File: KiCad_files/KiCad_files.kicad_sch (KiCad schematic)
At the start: 0 parts

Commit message: blablabla
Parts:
- added C1: 100nF, symbol Device:C
- added U1: ~, symbol New_Library:REF2033AIDDCT
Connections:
- new net: C1.1, U1. (V_REF)
- new net GND: C1.2, U1. (V_REF)

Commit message: test
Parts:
- added C2: 100nF, symbol Device:C
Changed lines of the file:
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@@
+	(symbol
+		(lib_id "Device:C")
+		(at 176.53 97.79 0)
+		(unit 1)
+		(exclude_from_sim no)
+		(in_bom yes)
+		(on_board yes)
+		(dnp no)
+		(fields_autoplaced yes)
+		(property "Reference" "C2"
+			(at 180.34 96.5199 0)
+			(effects
+				(font
+					(size 1.27 1.27)
+				)
+				(justify left)
+			)
+		)
+		(property "Value" "100nF"
+			(at 180.34 99.0599 0)
+			(effects
+				(font
+					(size 1.27 1.27)
+				)
+				(justify left)
+			)
+		)
+		(property "Footprint" ""
+			(at 177.4952 101.6 0)
+			(effects
+				(font
+					(size 1.27 1.27)
+				)
+				(hide yes)
+			)
+		)
+		(property "Datasheet" "~"
+			(at 176.53 97.79 0)
+			(effects
+				(font
+					(size 1.27 1.27)
+				)
+				(hide yes)
+			)
+		)
+		(property "Description" "Unpolarized capacitor"
+			(at 176.53 97.79 0)
+			(effects
+				(font
+					(size 1.27 1.27)
+				)
+				(hide yes)
+			)
+		)
+		(pin "2"
+		)
+		(pin "1"
+		)
+		(instances
+			(project "KiCad_files"
+				(path "/f93895fa-12b9-4ad7-81f4-36be00b56edd"
+					(reference "C2")
+					(unit 1)
+				)
+			)
+		)
+	)
 	(symbol
 		(lib_id "Device:C")

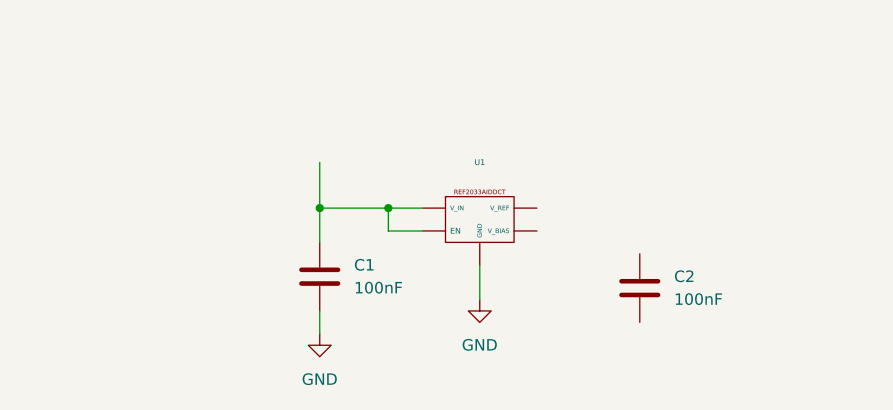
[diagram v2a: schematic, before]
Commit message: added the analog power supply to the main scheme
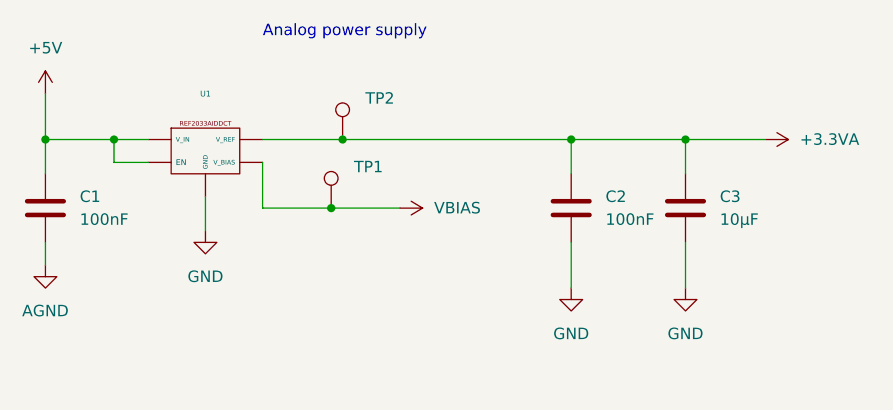
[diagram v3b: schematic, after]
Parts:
- added C3: 10μF, symbol Device:C
- added TP1, TP2: ~, symbol Connector:TestPoint
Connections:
- net GND: now also C2.2, C3.2; no longer C1.2
- net +3.3VA: now reaches C2.1
- net +3.3VA: now also U1. (V_REF), C3.1, TP2.1
- net +5V: now reaches C1.1, U1. (V_REF)
- net VBIAS: now reaches U1. (V_REF)
- net VBIAS: now also TP1.1
- new net AGND: C1.2
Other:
- note added: "Analog power supply"

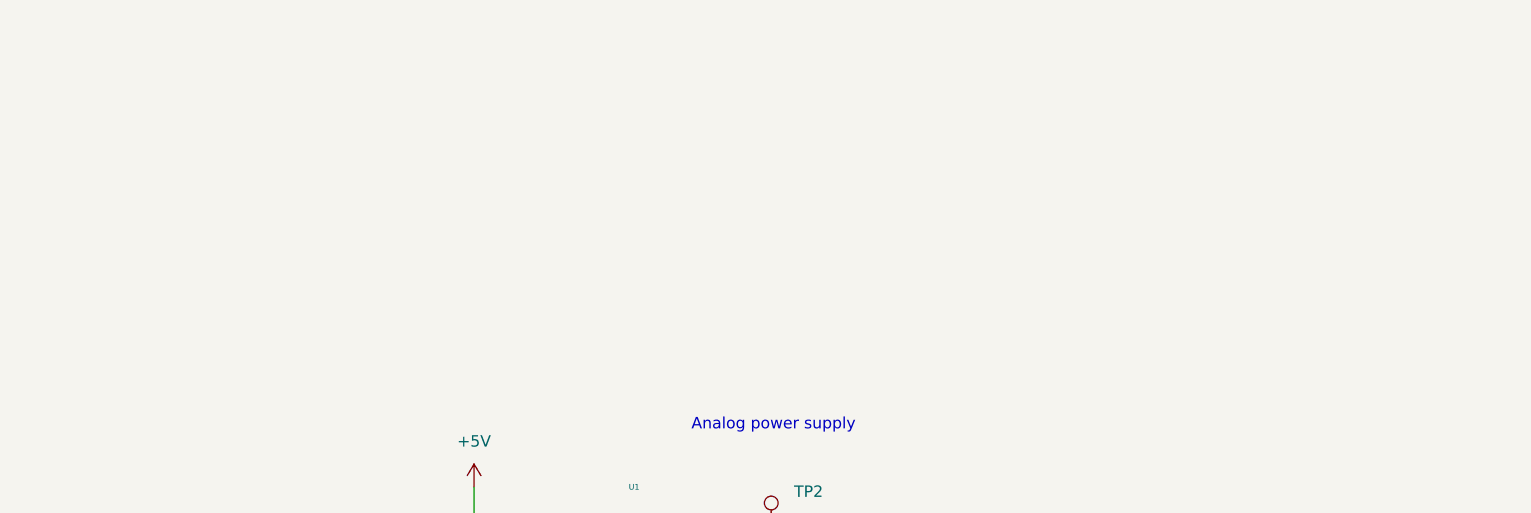
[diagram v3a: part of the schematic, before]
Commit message: Added digital power supply to schematic
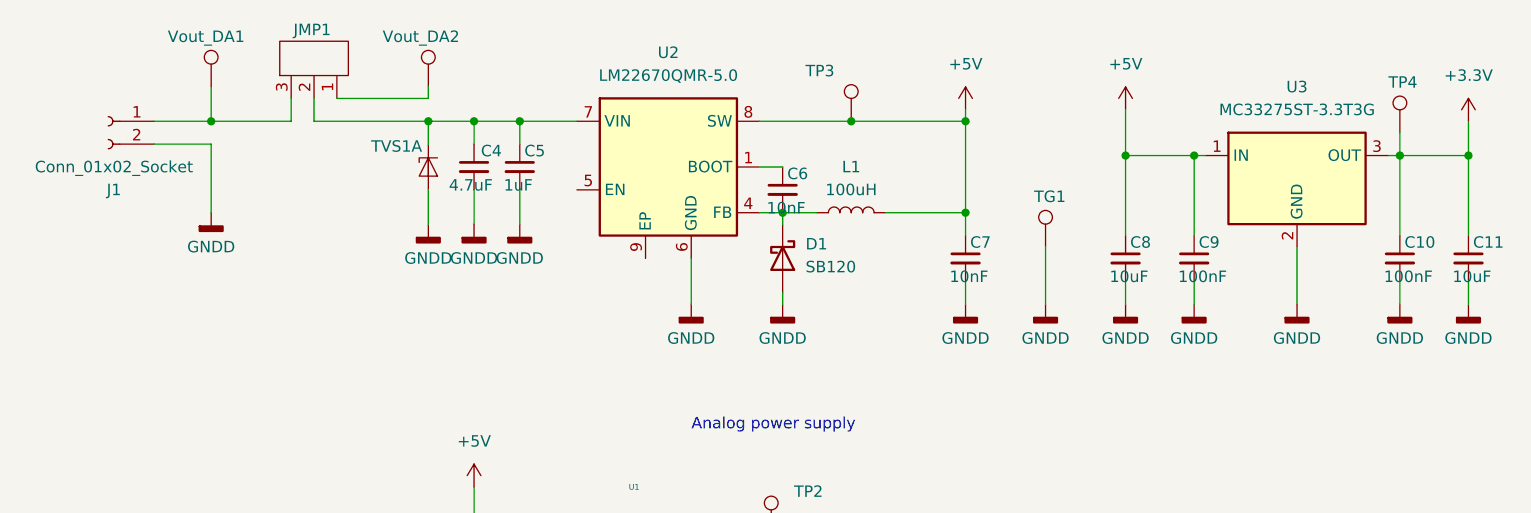
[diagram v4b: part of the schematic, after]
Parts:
- added C10, C9: 100nF, symbol Device:C_Small
- added C11, C8: 10uF, symbol Device:C_Small
- added C4: 4.7uF, symbol Device:C_Small
- added C5: 1uF, symbol Device:C_Small
- added C6, C7: 10nF, symbol Device:C_Small
- added D1: SB120, Diode_THT:D_DO-41_SOD81_P10.16mm_Horizontal, symbol Diode:SB120
- added J1: Conn_01x02_Socket, symbol Connector:Conn_01x02_Socket
- added JMP1: ~, symbol New_Library:3pin_jumper
- added L1: 100uH, symbol Device:L
- added TG1, TP3, TP4, Vout_DA1, Vout_DA2: TestPoint, symbol Connector:TestPoint
- added TVS1: PESD3V3U1UT, Package_TO_SOT_SMD:SOT-23, symbol Power_Protection:PESD3V3L4UF
- added U2: LM22670QMR-5.0, Package_SO:SOIC-8-1EP_3.9x4.9mm_P1.27mm_EP2.29x3mm, symbol Regulator_Switching:LM22676MR-5
- added U3: MC33275ST-3.3T3G, Package_TO_SOT_SMD:SOT-223, symbol Regulator_Linear:LT1963AxST-3.3
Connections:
- net +5V: now also C7.1, C8.1, C9.1, L1.2, TP3.1, U2.8 (SW), U3.1 (IN)
- new net: C4.1, C5.1, JMP1.2, TVS1.1 (K1), U2.7 (VIN)
- new net: JMP1.1, Vout_DA2.1
- new net: J1.1 (Pin_1), JMP1.3, Vout_DA1.1
- new net: C6.1, U2.1 (BOOT)
- new net: C6.2, D1.1 (K), L1.1, U2.4 (FB)
- new net +3.3V: C10.1, C11.1, TP4.1, U3.3 (OUT)
- new net GNDD: C10.2, C11.2, C4.2, C5.2, C7.2, C8.2, C9.2, D1.2 (A), J1.2 (Pin_2), TG1.1, TVS1.2 (A), TVS1.5 (A), U2.6 (GND), U3.2 (GND)

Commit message: minimal changes
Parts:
- removed Vout_DA1, Vout_DA2: TestPoint, symbol Connector:TestPoint
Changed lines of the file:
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@@
 	(wire
 		(pts
-			(xy 95.25 33.02) (xy 105.41 33.02)
+			(xy 95.25 33.02) (xy 101.6 33.02)
 		)
 		(stroke
@@
 	(wire
 		(pts
-			(xy 105.41 33.02) (xy 105.41 31.75)
+			(xy 101.6 33.02) (xy 101.6 30.48)
 		)
 		(stroke
@@
 	(wire
 		(pts
-			(xy 81.28 35.56) (xy 81.28 31.75)
+			(xy 81.28 35.56) (xy 81.28 30.48)
 		)
 		(stroke
@@
 		)
 	)
+	(netclass_flag ""
+		(length 2.54)
+		(shape round)
+		(at 101.6 30.48 0)
+		(effects
+			(font
+				(size 1.27 1.27)
+			)
+			(justify left bottom)
+		)
+		(property "Vin_DA15" ""
+			(at 96.774 25.908 0)
+			(show_name yes)
+			(effects
+				(font
+					(size 1.27 1.27)
+					(italic yes)
+				)
+				(justify left)
+			)
+		)
+	)
+	(netclass_flag ""
+		(length 2.54)
+		(shape round)
+		(at 81.28 30.48 0)
+		(effects
+			(font
+				(size 1.27 1.27)
+			)
+			(justify left bottom)
+		)
+		(property "Vout_DA15" ""
+			(at 75.946 25.908 0)
+			(show_name yes)
+			(effects
+				(font
+					(size 1.27 1.27)
+					(italic yes)
+				)
+				(justify left)
+			)
+		)
+	)
 	(symbol
 		(lib_id "power:GND")
@@
 	)
 	(symbol
-		(lib_id "Connector:TestPoint")
-		(at 105.41 31.75 0)
-		(unit 1)
-		(exclude_from_sim no)
-		(in_bom yes)
-		(on_board yes)
-		(dnp no)
-		(property "Reference" "Vout_DA2"
-			(at 100.33 26.162 0)
-			(effects
-				(font
-					(size 1.27 1.27)
-				)
-				(justify left)
-			)
-		)
-		(property "Value" "TestPoint"
-			(at 107.95 29.7179 0)
-			(effects
-				(font
-					(size 1.27 1.27)
-				)
-				(justify left)
-				(hide yes)
-			)
-		)
-		(property "Footprint" ""
-			(at 110.49 31.75 0)
-			(effects
-				(font
-					(size 1.27 1.27)
-				)
-				(hide yes)
-			)
-		)
-		(property "Datasheet" "~"
-			(at 110.49 31.75 0)
-			(effects
-				(font
-					(size 1.27 1.27)
-				)
-				(hide yes)
-			)
-		)
-		(property "Description" "test point"
-			(at 105.41 31.75 0)
-			(effects
-				(font
-					(size 1.27 1.27)
-				)
-				(hide yes)
-			)
-		)
-		(pin "1"
-		)
-		(instances
-			(project "KiCad_files"
-				(path "/f93895fa-12b9-4ad7-81f4-36be00b56edd"
-					(reference "Vout_DA2")
-					(unit 1)
-				)
-			)
-		)
-	)
-	(symbol
 		(lib_id "Device:C_Small")
 		(at 165.1 50.8 0)
@@
 					(unit 1)
 				)
-			)
-		)
-	)
-	(symbol
-		(lib_id "Connector:TestPoint")
-		(at 81.28 31.75 0)
-		(unit 1)
-		(exclude_from_sim no)
-		(in_bom yes)
-		(on_board yes)
-		(dnp no)
-		(property "Reference" "Vout_DA1"
-			(at 76.454 26.162 0)
-			(effects
-				(font
-					(size 1.27 1.27)
-				)
-				(justify left)
-			)
-		)
-		(property "Value" "TestPoint"
-			(at 83.82 29.7179 0)
-			(effects
-				(font
-					(size 1.27 1.27)
-				)
-				(justify left)
-				(hide yes)
-			)
-		)
-		(property "Footprint" ""
-			(at 86.36 31.75 0)
-			(effects
-				(font
-					(size 1.27 1.27)
-				)
-				(hide yes)
-			)
-		)
-		(property "Datasheet" "~"
-			(at 86.36 31.75 0)
-			(effects
-				(font
-					(size 1.27 1.27)
-				)
-				(hide yes)
-			)
-		)
-		(property "Description" "test point"
-			(at 81.28 31.75 0)
-			(effects
-				(font
-					(size 1.27 1.27)
-				)
-				(hide yes)
-			)
-		)
-		(pin "1"
-		)
-		(instances
-			(project "KiCad_files"
-				(path "/f93895fa-12b9-4ad7-81f4-36be00b56edd"
-					(reference "Vout_DA1")
-					(unit 1)
-				)

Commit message: i changed the ground to gnda on the analog power supply
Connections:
- net GND is gone; now on net GNDA: C2.2, C3.2, U1. (V_REF)
- net AGND renamed GNDA
- net VBIAS: no longer names the net of TP1.1, U1. (V_REF)

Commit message: i inserted the RS422 communication circuit to the mains scheme
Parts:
- added C12: 100nF, symbol Device:C
- added J10, J11: Conn_01x01_Pin, symbol Connector:Conn_01x01_Pin
- added J2, J4: ~, symbol Connector:Conn_01x02_Socket
- added J3, J5: ~, symbol Connector:Conn_01x04_Socket
- added J6, J7, J8, J9: Conn_01x01_Socket, symbol Connector:Conn_01x01_Socket
- added R1: 120, symbol Device:R
- added R2: R, symbol Device:R
- added R3, R4: 68, symbol Device:R
- added TP10, TP11, TP5, TP6, TP7, TP8, TP9: TestPoint, symbol Connector:TestPoint
- added U4: ADM3488ExR, Package_SO:SOIC-8_3.9x4.9mm_P1.27mm, symbol Interface_UART:ADM3488ExR
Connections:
- net +3.3V: now also C12.1, U4.1 (VCC)
- net GNDD: now also C12.2, J3.1 (Pin_1), J3.2 (Pin_2), J3.3 (Pin_3), J3.4 (Pin_4), J5.1 (Pin_1), J5.2 (Pin_2), J5.3 (Pin_3), J5.4 (Pin_4), TP11.1, U4.4 (GND)
- new net: J4.1 (Pin_1), J4.2 (Pin_2)
- new net: R4.1, TP10.1, U4.3 (DI)
- new net: J11.1 (Pin_1), R4.2
- new net: J6.1 (Pin_1), R1.1, TP5.1, U4.8 (A)
- new net: J7.1 (Pin_1), R1.2, TP6.1, U4.7 (B)
- new net: J8.1 (Pin_1), R2.1, TP7.1, U4.6 (Z)
- new net: J9.1 (Pin_1), R2.2, TP8.1, U4.5 (Y)
- new net: R3.1, TP9.1, U4.2 (RO)
- new net: J10.1 (Pin_1), R3.2
- new net: J2.1 (Pin_1), J2.2 (Pin_2)
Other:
- moved on the sheet: C1, C2, C3, TP1, TP2, U1

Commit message: The switch Module done!
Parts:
- added D2: D, symbol Device:D
- added D3: D_Zener, symbol Device:D_Zener
- added MB1: ~, symbol Connector:Conn_01x01_Pin
- added R5: 330, symbol Device:R
- added R6: 47k, symbol Device:R
- added SW1: SW_Omron_B3FS, symbol Switch:SW_Omron_B3FS
- added TP12: ~, symbol Connector:TestPoint
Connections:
- net +3.3V: now also R6.1
- net GNDD: now also D2.2 (A), D3.2 (A), SW1.2
- new net: D2.1 (K), D3.1 (K), R5.2, R6.2, SW1.1, TP12.1
- new net: MB1.1 (Pin_1), R5.1
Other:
- note added: "(I could not find TVS2 PED3V3U1UT)"
- note added: "(I could not find the correct switch, namely the WE430182070816)"
- note added: "Switch Module"
